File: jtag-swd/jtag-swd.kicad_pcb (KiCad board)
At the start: 2 copper layers, 16.5 x 12.7 mm, 3 parts, among them J1 Conn_ARM_JTAG_SWD_10, J2 Conn_01x04_Male, J3 Conn_01x02_Male

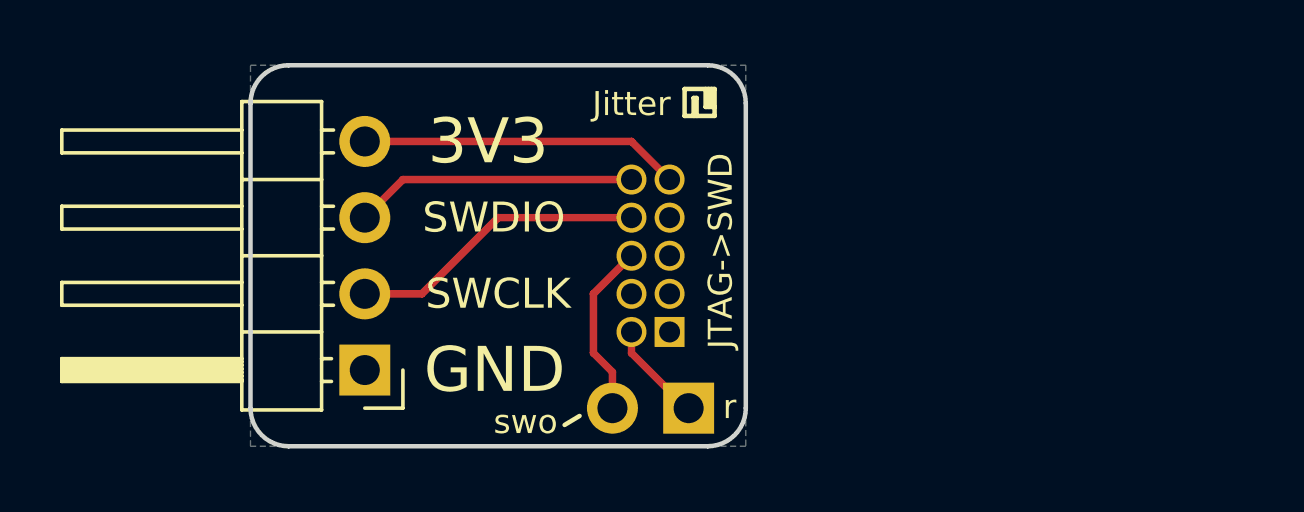
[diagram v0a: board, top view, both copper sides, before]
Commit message: Add USB MITM board and update jtag-swd adapter
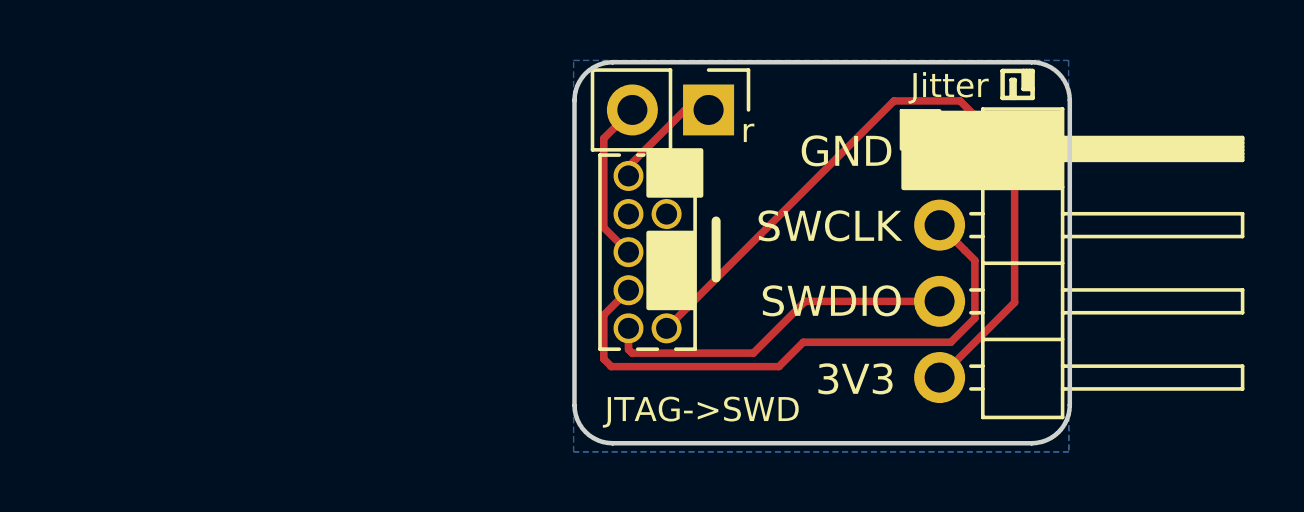
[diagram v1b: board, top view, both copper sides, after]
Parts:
- J1: moved to F.Cu
- J3: footprint Jitter_Footprints:PinHeader_1x02_P2.54mm_Vertical_no_silk -> Connector_PinHeader_2.54mm:PinHeader_1x02_P2.54mm_Vertical
- moved J2 20.5 mm to (85.2, 44.7), turned to 0 degrees
- moved J3 9.96 mm to (77.5, 43.4)
- moved J1 5.20 mm to (76.1, 45.6)
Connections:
- J1 pad 9: (no net) -> GND
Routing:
- net +3V3: track 10.7 -> 23.9 mm
- net /SWCLK: track 9.94 -> 19.4 mm
- net /SWDIO: track 9.42 -> 11.8 mm
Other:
- board text added: "3v3"
- board text added: "swclk"
- board text added: "swdio"
